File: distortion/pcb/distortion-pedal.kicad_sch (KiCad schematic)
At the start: 24 parts, among them U2 TL081H, U4 TL081H

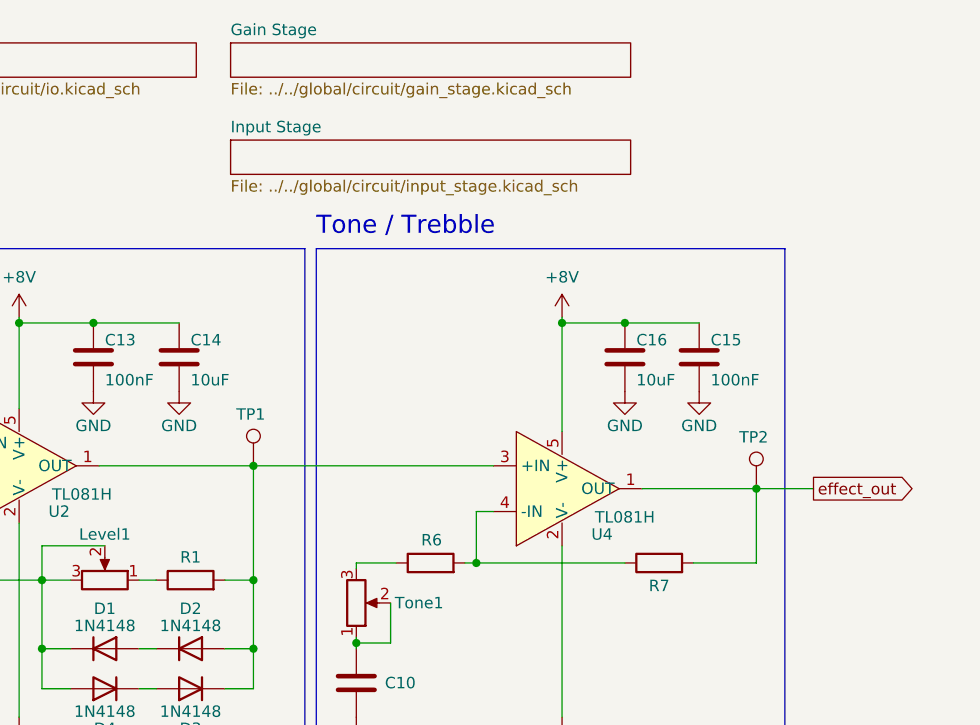
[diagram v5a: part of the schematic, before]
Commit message: minor circuit rework for better use with multiple projects
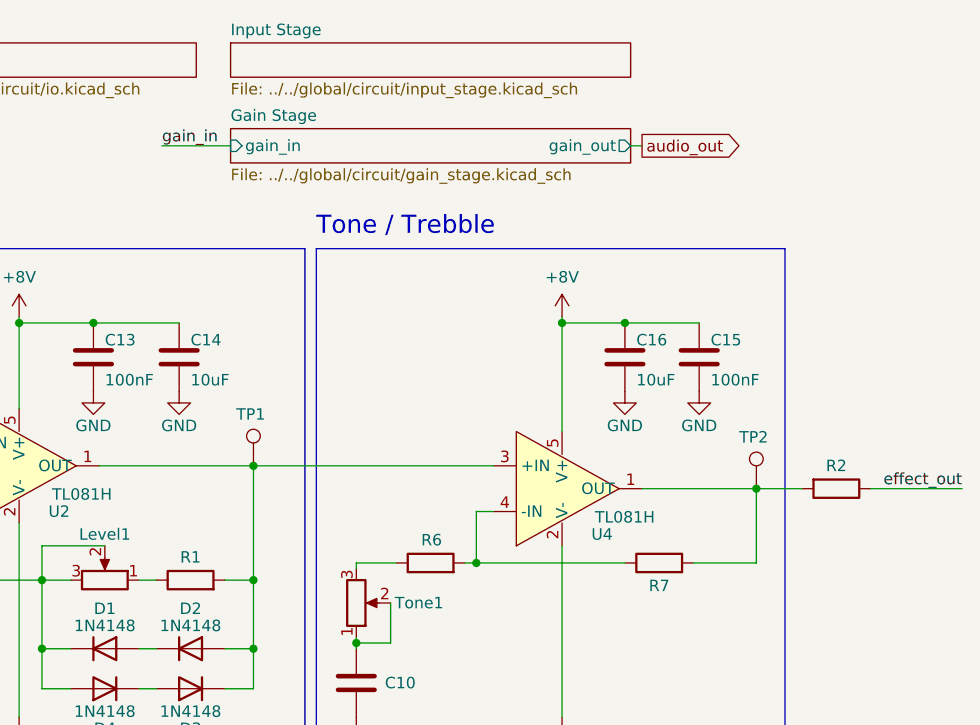
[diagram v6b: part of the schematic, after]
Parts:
- added R2: R, Resistor_SMD:R_0805_2012Metric_Pad1.20x1.40mm_HandSolder, symbol Device:R
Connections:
- net effect_out: now also R2.1; no longer R7.2, TP2.1, U4.1 (OUT)
- new net: R2.2, R7.2, TP2.1, U4.1 (OUT)
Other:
- sheet Gain Stage ports: added gain_in, gain_out; removed none
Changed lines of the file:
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@@
+    (stroke (width 0) (type default) (color 0 0 0 0))
+  )
+  (wire (pts (xy 168.275 68.58) (xy 173.355 68.58))
     (stroke (width 0) (type default) (color 0 0 0 0))
   )
@@
     (stroke (width 0) (type default) (color 0 0 0 0))
   )
+  (wire (pts (xy 168.275 68.58) (xy 168.275 76.835))
+    (stroke (width 0) (type default) (color 0 0 0 0))
+  )
   (wire (pts (xy 94.615 50.165) (xy 104.14 50.165))
     (stroke (width 0) (type default) (color 0 0 0 0))
@@
     (stroke (width 0) (type default) (color 0 0 0 0))
   )
-  (wire (pts (xy 168.275 68.58) (xy 174.625 68.58))
-    (stroke (width 0) (type default) (color 0 0 0 0))
-  )
   (wire (pts (xy 45.085 60.96) (xy 45.085 63.5))
     (stroke (width 0) (type default) (color 0 0 0 0))
@@
     (stroke (width 0) (type default) (color 0 0 0 0))
   )
+  (wire (pts (xy 102.235 30.48) (xy 109.855 30.48))
+    (stroke (width 0) (type default) (color 0 0 0 0))
+  )
   (wire (pts (xy 99.695 90.805) (xy 101.6 90.805))
     (stroke (width 0) (type default) (color 0 0 0 0))
@@
     (stroke (width 0) (type default) (color 0 0 0 0))
   )
-  (wire (pts (xy 168.275 76.835) (xy 168.275 68.58))
-    (stroke (width 0) (type default) (color 0 0 0 0))
-  )
   (polyline (pts (xy 171.45 101.6) (xy 171.45 41.91))
     (stroke (width 0) (type default) (color 0 0 0 0))
@@
     (stroke (width 0) (type default) (color 0 0 0 0))
   )
+  (wire (pts (xy 154.305 30.48) (xy 155.575 30.48))
+    (stroke (width 0) (type default) (color 0 0 0 0))
+  )
   (wire (pts (xy 86.36 50.165) (xy 86.36 59.69))
     (stroke (width 0) (type default) (color 0 0 0 0))
@@
   )
   (wire (pts (xy 123.825 76.835) (xy 128.27 76.835))
+    (stroke (width 0) (type default) (color 0 0 0 0))
+  )
+  (wire (pts (xy 180.975 68.58) (xy 191.135 68.58))
     (stroke (width 0) (type default) (color 0 0 0 0))
   )
@@
     (effects (font (size 1.27 1.27)) (justify left bottom))
   )
-  (global_label "effect_out" (shape output) (at 174.625 68.58 0) (fields_autoplaced)
+  (label "effect_out" (at 191.135 68.58 180)
+    (effects (font (size 1.27 1.27)) (justify right bottom))
+  )
+  (label "gain_in" (at 102.235 30.48 0)
+    (effects (font (size 1.27 1.27)) (justify left bottom))
+  )
+  (global_label "audio_out" (shape output) (at 155.575 30.48 0) (fields_autoplaced)
     (effects (font (size 1.27 1.27)) (justify left))
-    (property "Intersheet References" "${INTERSHEET_REFS}" (id 0) (at 186.4724 68.5006 0)
+    (property "Intersheet References" "${INTERSHEET_REFS}" (id 0) (at 167.1805 30.4006 0)
       (effects (font (size 1.27 1.27)) (justify left) hide)
     )
@@
     )
     (property "Datasheet" "~" (id 3) (at 68.58 77.47 0)
+      (effects (font (size 1.27 1.27)) hide)
+    )
+    (pin "1")
+    (pin "2")
+  )
+  (symbol (lib_id "Device:R") (at 177.165 68.58 270) (unit 1)
+    (in_bom yes) (on_board yes)
+    (property "Reference" "R2" (id 0) (at 177.165 66.04 90))
+    (property "Value" "R" (id 1) (at 177.165 64.135 90)
+      (effects (font (size 1.27 1.27)) hide)
+    )
+    (property "Footprint" "Resistor_SMD:R_0805_2012Metric_Pad1.20x1.40mm_HandSolder" (id 2) (at 177.165 66.802 90)
+      (effects (font (size 1.27 1.27)) hide)
+    )
+    (property "Datasheet" "~" (id 3) (at 177.165 68.58 0)
       (effects (font (size 1.27 1.27)) hide)
     )
@@
     )
   )
-  (sheet (at 109.855 29.845) (size 44.45 3.81) (fields_autoplaced)
+  (sheet (at 109.855 19.05) (size 44.45 3.81) (fields_autoplaced)
     (stroke (width 0.1524) (type solid) (color 0 0 0 0))
     (fill (color 0 72 72 1.0000))
-    (property "Sheet name" "Input Stage" (id 0) (at 109.855 29.1334 0)
+    (property "Sheet name" "Input Stage" (id 0) (at 109.855 18.3384 0)
       (effects (font (size 1.27 1.27)) (justify left bottom))
     )
-    (property "Sheet file" "../../global/circuit/input_stage.kicad_sch" (id 1) (at 109.855 34.2396 0)
+    (property "Sheet file" "../../global/circuit/input_stage.kicad_sch" (id 1) (at 109.855 23.4446 0)
       (effects (font (size 1.27 1.27)) (justify left top))
     )
@@
     )
   )
-  (sheet (at 109.855 19.05) (size 44.45 3.81) (fields_autoplaced)
+  (sheet (at 109.855 28.575) (size 44.45 3.81) (fields_autoplaced)
     (stroke (width 0.1524) (type solid) (color 0 0 0 0))
     (fill (color 0 72 72 1.0000))
-    (property "Sheet name" "Gain Stage" (id 0) (at 109.855 18.3384 0)
+    (property "Sheet name" "Gain Stage" (id 0) (at 109.855 27.8634 0)
       (effects (font (size 1.27 1.27)) (justify left bottom))
     )
-    (property "Sheet file" "../../global/circuit/gain_stage.kicad_sch" (id 1) (at 109.855 23.4446 0)
+    (property "Sheet file" "../../global/circuit/gain_stage.kicad_sch" (id 1) (at 109.855 32.9696 0)
       (effects (font (size 1.27 1.27)) (justify left top))
+    )
+    (pin "gain_out" output (at 154.305 30.48 0)
+      (effects (font (size 1.27 1.27)) (justify right))
+    )
+    (pin "gain_in" input (at 109.855 30.48 180)
+      (effects (font (size 1.27 1.27)) (justify left))
     )
   )
@@
       (reference "R1") (unit 1) (value "R") (footprint "Resistor_SMD:R_0805_2012Metric_Pad1.20x1.40mm_HandSolder")
     )
-    (path "/f6017cd5-478f-4689-9d02-df19f7bba10d/834acd1c-5fe0-43dc-ba9b-fcba03c469ca"
+    (path "/9979a8b0-0b59-4b9a-99ae-49e16c8df7a6"
       (reference "R2") (unit 1) (value "R") (footprint "Resistor_SMD:R_0805_2012Metric_Pad1.20x1.40mm_HandSolder")
     )
@@
       (reference "TP5") (unit 1) (value "TestPoint") (footprint "TestPoint:TestPoint_THTPad_1.0x1.0mm_Drill0.5mm")
     )
-    (path "/f6017cd5-478f-4689-9d02-df19f7bba10d/a837afde-7834-4371-98f7-88fcc412f904"
-      (reference "TP6") (unit 1) (value "TestPoint") (footprint "TestPoint:TestPoint_THTPad_1.0x1.0mm_Drill0.5mm")
-    )
     (path "/ba5ce591-bab6-4a4e-a26c-dee07b815b67/7c524ad3-08fd-470a-9543-ad19dbc5596a"
